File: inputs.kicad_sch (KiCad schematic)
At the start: 14 parts

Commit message: Changed optocoupler resistor values, updated Mouser PNs
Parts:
- C11, C3, C4, C7, C8: Mauser PN 80-C0805C103J5R -> (none); Mouser PN (none) -> 80-C0805C103J5R
- CRUZ_SET_SW1, REGENSW1: Mauser PN 538-43650-0215 -> (none); Mouser PN (none) -> 538-43650-0215
- F/R_SW1: Mauser PN 538-43650-0415 -> (none); Mouser PN (none) -> 538-43650-0415
- R12, R2, R3, R6, R7: Mauser PN 71-CRCW080510K0FKEAC -> (none); Mouser PN (none) -> 71-CRCW080510K0FKEAC
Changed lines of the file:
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@@
       (effects (font (size 1.27 1.27)) hide)
     )
-    (property "Mauser PN" "80-C0805C103J5R" (at 43.815 113.03 0)
+    (property "Mouser PN" "80-C0805C103J5R" (at 43.815 113.03 0)
       (effects (font (size 1.27 1.27)) hide)
     )
@@
       (effects (font (size 1.27 1.27)) hide)
     )
-    (property "Mauser PN" "80-C0805C103J5R" (at 198.12 109.22 0)
+    (property "Mouser PN" "80-C0805C103J5R" (at 198.12 109.22 0)
       (effects (font (size 1.27 1.27)) hide)
     )
@@
       (effects (font (size 1.27 1.27)) hide)
     )
-    (property "Mauser PN" "538-43650-0215" (at 93.345 103.505 0)
+    (property "Mouser PN" "538-43650-0215" (at 93.345 103.505 0)
       (effects (font (size 1.27 1.27)) hide)
     )
@@
       (effects (font (size 1.27 1.27)) hide)
     )
-    (property "Mauser PN" "538-43650-0215" (at 142.24 106.045 0)
+    (property "Mouser PN" "538-43650-0215" (at 142.24 106.045 0)
       (effects (font (size 1.27 1.27)) hide)
     )
@@
       (effects (font (size 1.27 1.27)) hide)
     )
-    (property "Mauser PN" "80-C0805C103J5R" (at 89.535 116.84 0)
+    (property "Mouser PN" "80-C0805C103J5R" (at 89.535 116.84 0)
       (effects (font (size 1.27 1.27)) hide)
     )
@@
       (effects (font (size 1.27 1.27)) hide)
     )
-    (property "Mauser PN" "71-CRCW080510K0FKEAC " (at 142.24 116.84 0)
+    (property "Mouser PN" "71-CRCW080510K0FKEAC " (at 142.24 116.84 0)
       (effects (font (size 1.27 1.27)) hide)
     )
@@
       (effects (font (size 1.27 1.27)) hide)
     )
-    (property "Mauser PN" "538-43650-0215" (at 47.625 101.6 0)
+    (property "Mouser PN" "538-43650-0215" (at 47.625 101.6 0)
       (effects (font (size 1.27 1.27)) hide)
     )
@@
       (effects (font (size 1.27 1.27)) hide)
     )
-    (property "Mauser PN" "538-43650-0415" (at 191.135 122.555 0)
+    (property "Mouser PN" "538-43650-0415" (at 191.135 122.555 0)
       (effects (font (size 1.27 1.27)) hide)
     )
@@
       (effects (font (size 1.27 1.27)) hide)
     )
-    (property "Mauser PN" "71-CRCW080510K0FKEAC " (at 208.28 109.22 0)
+    (property "Mouser PN" "71-CRCW080510K0FKEAC " (at 208.28 109.22 0)
       (effects (font (size 1.27 1.27)) hide)
     )
@@
       (effects (font (size 1.27 1.27)) hide)
     )
-    (property "Mauser PN" "80-C0805C103J5R" (at 215.265 109.22 0)
+    (property "Mouser PN" "80-C0805C103J5R" (at 215.265 109.22 0)
       (effects (font (size 1.27 1.27)) hide)
     )
@@
       (effects (font (size 1.27 1.27)) hide)
     )
-    (property "Mauser PN" "71-CRCW080510K0FKEAC " (at 47.625 113.665 0)
+    (property "Mouser PN" "71-CRCW080510K0FKEAC " (at 47.625 113.665 0)
       (effects (font (size 1.27 1.27)) hide)
     )
@@
       (effects (font (size 1.27 1.27)) hide)
     )
-    (property "Mauser PN" "71-CRCW080510K0FKEAC " (at 93.345 116.84 0)
+    (property "Mouser PN" "71-CRCW080510K0FKEAC " (at 93.345 116.84 0)
       (effects (font (size 1.27 1.27)) hide)
     )
@@
       (effects (font (size 1.27 1.27)) hide)
     )
-    (property "Mauser PN" "80-C0805C103J5R" (at 138.43 116.84 0)
+    (property "Mouser PN" "80-C0805C103J5R" (at 138.43 116.84 0)
       (effects (font (size 1.27 1.27)) hide)
     )
@@
       (effects (font (size 1.27 1.27)) hide)
     )
-    (property "Mauser PN" "71-CRCW080510K0FKEAC " (at 191.135 109.22 0)
-      (effects (font (size 1.27 1.27)) hide)
-    )
+    (property "Mouser PN" "71-CRCW080510K0FKEAC " (at 191.135 109.22 0)
+      (effects (font (size 1.27 1.27)) hide)
+    )

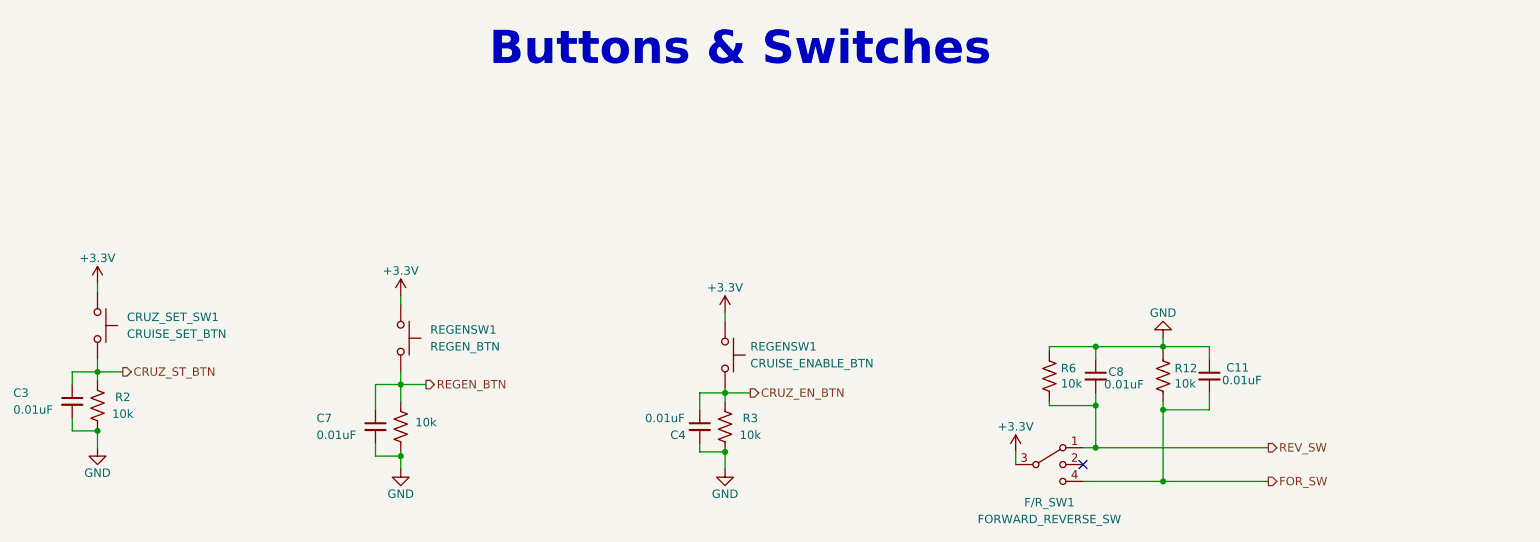
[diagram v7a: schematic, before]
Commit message: Added I2C GPIO expander to reduce GPIO pins from LeaderSOM and replace 555 timer circuit. Adjusted ignition switch signals.
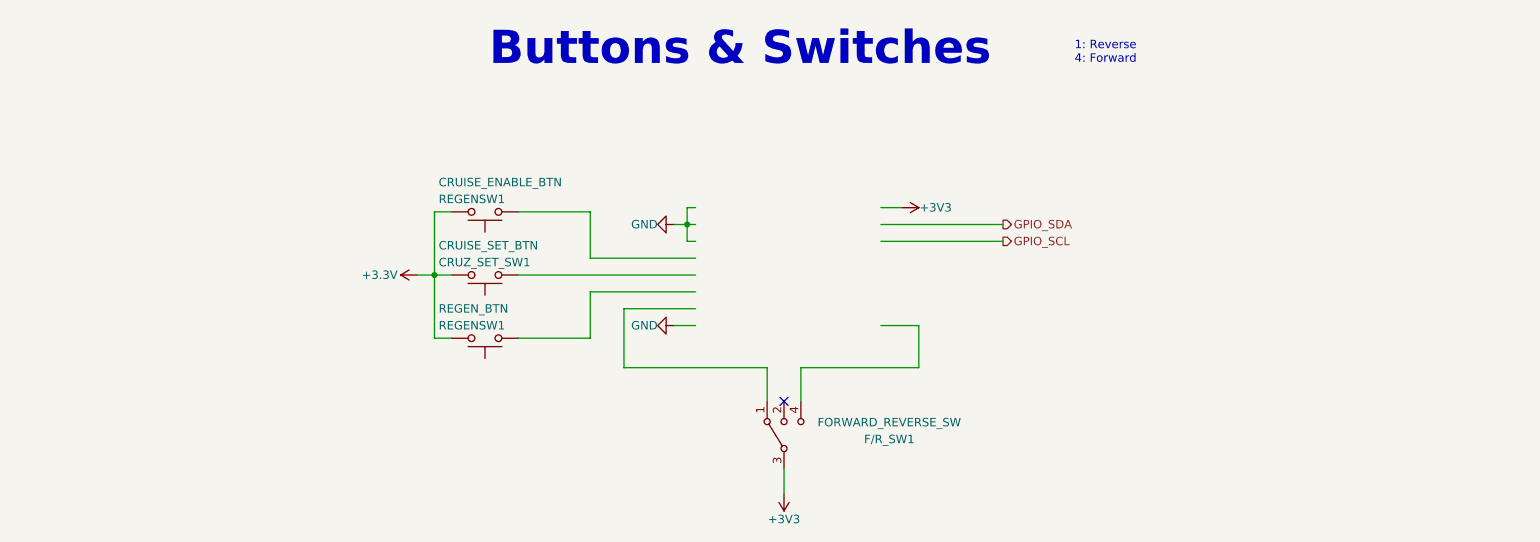
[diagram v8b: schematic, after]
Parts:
- removed C11, C3, C4, C7, C8: 0.01uF, Capacitor_SMD:C_0805_2012Metric, symbol Device:C_Small
- removed R12, R2, R3, R6, R7: 10k, Resistor_SMD:R_0805_2012Metric, symbol Device:R_US
- removed REGENSW1: REGEN_BTN, Connector_Molex:Molex_Micro-Fit_3.0_43650-0215_1x02_P3.00mm_Vertical, symbol Switch:SW_Push
- removed REGENSW1: CRUISE_ENABLE_BTN, Connector_Molex:Molex_Micro-Fit_3.0_43650-0215_1x02_P3.00mm_Vertical, symbol Switch:SW_Push
- added REGENSW1: REGEN_BTN, Connector_Molex:Molex_Micro-Fit_3.0_43650-0215_1x02_P3.00mm_Vertical, symbol Switch:SW_Push
- added REGENSW1: CRUISE_ENABLE_BTN, Connector_Molex:Molex_Micro-Fit_3.0_43650-0215_1x02_P3.00mm_Vertical, symbol Switch:SW_Push
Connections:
- net CRUZ_ST_BTN is gone; now on net +3.3V: CRUZ_SET_SW1.2
- net +3.3V: now also REGENSW1.2, REGENSW1.2; no longer CRUZ_SET_SW1.1, F/R_SW1.3
- net FOR_SW: no longer names the net of F/R_SW1.4
- net REV_SW: no longer names the net of F/R_SW1.1
- new net +3V3: F/R_SW1.3
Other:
- note added: "1: Reverse 4: Forward"
